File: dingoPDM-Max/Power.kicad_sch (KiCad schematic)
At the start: 14 parts, among them U1 VXO780x-500-M, U2 LD1117S33CTR

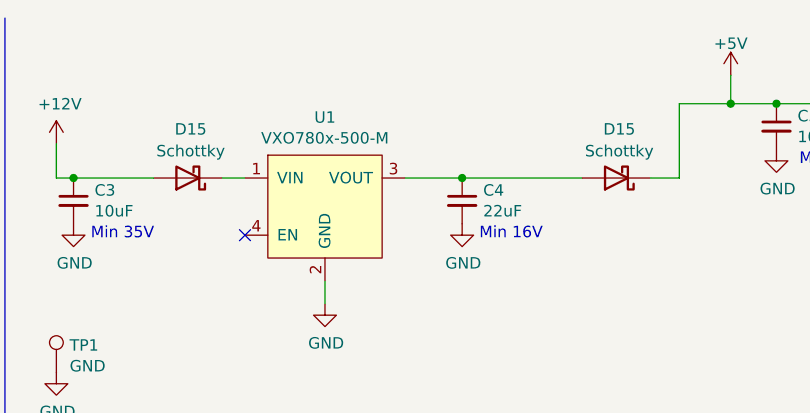
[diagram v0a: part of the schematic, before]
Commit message: Updated to Kicad 8
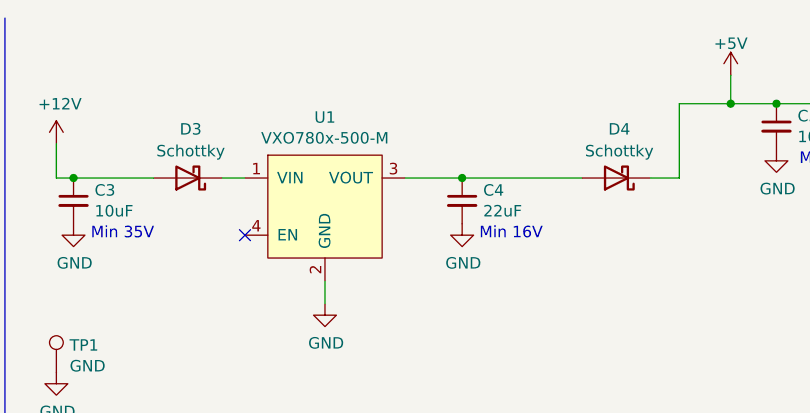
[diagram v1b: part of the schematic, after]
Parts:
- renumbered D15 to D3, D15 to D4

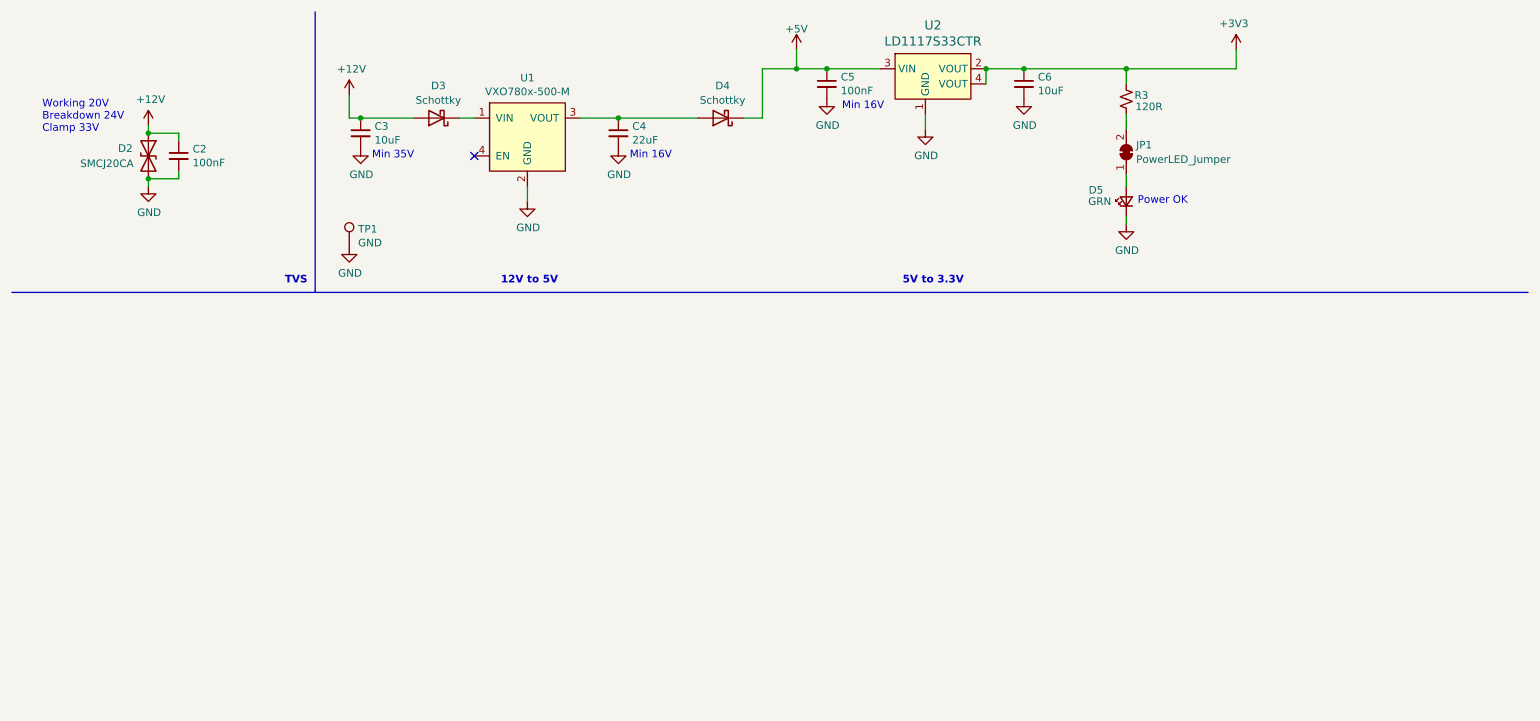
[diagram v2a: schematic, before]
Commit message: add dc-dc options and 5v cap
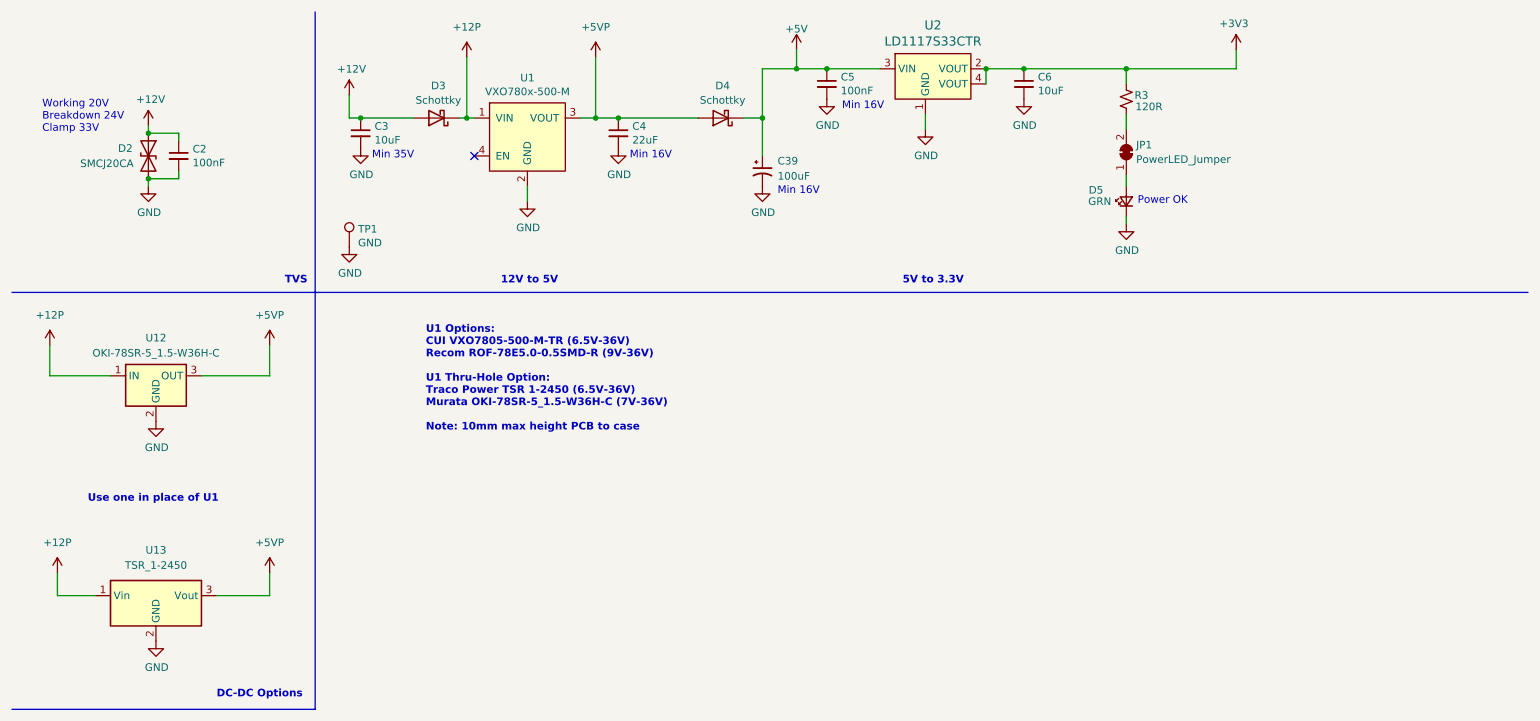
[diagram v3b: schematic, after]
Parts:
- added C39: 100uF, Capacitor_SMD:CP_Elec_6.3x7.7, symbol Device:C_Polarized_Small_US
- added U12: OKI-78SR-5_1.5-W36H-C, Converter_DCDC:Converter_DCDC_Murata_OKI-78SR_Horizontal, symbol Converter_DCDC:OKI-78SR-5_1.5-W36H-C
- added U13: TSR_1-2450, Converter_DCDC:Converter_DCDC_TRACO_TSR-1_THT, symbol Regulator_Switching:TSR_1-2450
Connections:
- net +5V: now also C39.1
- net GND: now also C39.2, U12.2 (GND), U13.2 (GND)
- net +12P: now reaches D3.1 (K), U1.1 (VIN)
- net +12P: now also U12.1 (IN), U13.1 (Vin)
- net +5VP: now reaches C4.1, D4.2 (A), U1.3 (VOUT)
- net +5VP: now also U12.3 (OUT), U13.3 (Vout)
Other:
- note added: "DC-DC Options"
- note added: "U1 Options: CUI VXO7805-500-M-TR (6.5V-36V) Recom ROF-78E5.0-0.5SMD-R (9V-36V) U1 Thru-Hole Option: Traco Power TSR 1-2450 (6.5V-36V) Murata OKI-78SR-5_1.5-W36H-C (7V-36V) Note: 10mm max height PCB to case"
- note added: "Use one in place of U1"

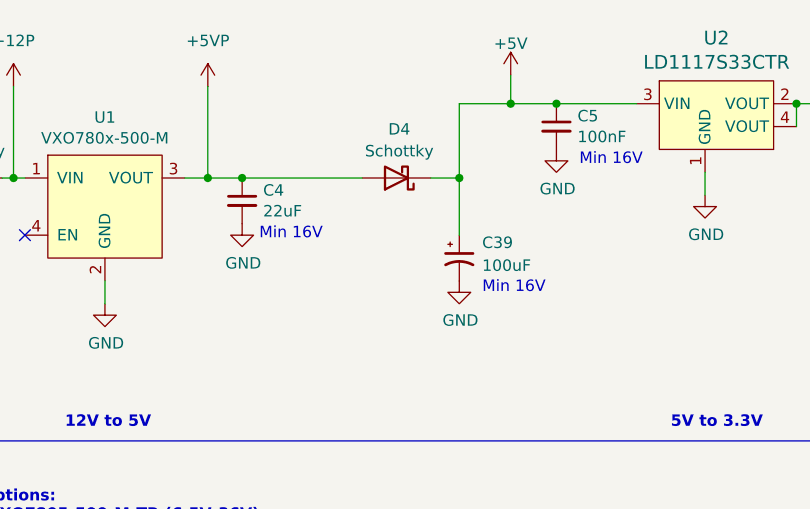
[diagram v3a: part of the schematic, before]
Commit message: switch to ceramic caps
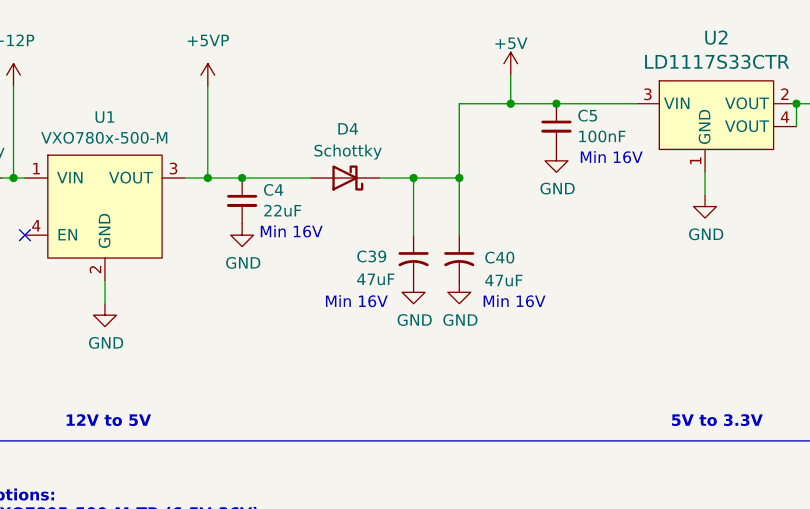
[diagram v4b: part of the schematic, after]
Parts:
- added C40: 47uF, Capacitor_SMD:C_2220_5750Metric, symbol Device:C_Small_US
- C39: value 100uF -> 47uF; footprint Capacitor_SMD:CP_Elec_6.3x7.7 -> Capacitor_SMD:C_2220_5750Metric; symbol Device:C_Polarized_Small_US -> Device:C_Small_US; Digi-Key_PN (none) -> 445-7935-1-ND
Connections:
- net +5V: now also C40.1
- net GND: now also C40.2
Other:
- moved on the sheet: D4
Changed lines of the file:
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@@
 	(text "Min 16V"
 		(exclude_from_sim no)
-		(at 140.97 44.704 0)
+		(at 123.444 46.482 0)
 		(effects
 			(font
@@
 		)
 	)
+	(text "Min 16V"
+		(exclude_from_sim no)
+		(at 140.97 46.482 0)
+		(effects
+			(font
+				(size 1.27 1.27)
+			)
+			(justify left bottom)
+		)
+	)
 	(text "DC-DC Options"
 		(exclude_from_sim no)
@@
 	)
 	(junction
+		(at 133.35 31.75)
+		(diameter 0)
+		(color 0 0 0 0)
+	)
+	(junction
 		(at 110.49 31.75)
 		(diameter 0)
@@
 	(wire
 		(pts
-			(xy 138.43 31.75) (xy 138.43 38.1)
+			(xy 133.35 31.75) (xy 133.35 38.1)
 		)
 		(stroke
@@
 	(wire
 		(pts
-			(xy 135.255 31.75) (xy 138.43 31.75)
+			(xy 129.54 31.75) (xy 133.35 31.75)
 		)
 		(stroke
@@
 		)
 	)
+	(wire
+		(pts
+			(xy 138.43 31.75) (xy 138.43 38.1)
+		)
+		(stroke
+			(width 0)
+			(type default)
+		)
+	)
 	(polyline
 		(pts
@@
 	(wire
 		(pts
-			(xy 114.3 31.75) (xy 127.635 31.75)
+			(xy 114.3 31.75) (xy 121.92 31.75)
 		)
 		(stroke
@@
 	(wire
 		(pts
+			(xy 133.35 31.75) (xy 138.43 31.75)
+		)
+		(stroke
+			(width 0)
+			(type default)
+		)
+	)
+	(wire
+		(pts
 			(xy 55.88 74.93) (xy 55.88 69.85)
 		)
@@
 	(symbol
 		(lib_id "Device:D_Schottky")
-		(at 131.445 31.75 180)
+		(at 125.73 31.75 180)
 		(unit 1)
 		(exclude_from_sim no)
@@
 		(fields_autoplaced yes)
 		(property "Reference" "D4"
-			(at 131.7625 26.3357 0)
+			(at 126.0475 26.3357 0)
 			(effects
 				(font
@@
 		)
 		(property "Value" "Schottky"
-			(at 131.7625 28.7599 0)
+			(at 126.0475 28.7599 0)
 			(effects
 				(font
@@
 		)
 		(property "Footprint" "Diode_SMD:D_SOD-123"
-			(at 131.445 31.75 0)
+			(at 125.73 31.75 0)
 			(effects
 				(font
@@
 		)
 		(property "Datasheet" ""
-			(at 131.445 31.75 0)
+			(at 125.73 31.75 0)
 			(effects
 				(font
@@
 		)
 		(property "Description" ""
-			(at 131.445 31.75 0)
+			(at 125.73 31.75 0)
 			(effects
 				(font
@@
 		)
 		(property "Digi-Key_PN" "1727-2394-1-ND"
-			(at 131.445 31.75 0)
+			(at 125.73 31.75 0)
 			(effects
 				(font
@@
 		)
 		(property "LCSC" "C179426"
-			(at 131.445 31.75 0)
+			(at 125.73 31.75 0)
 			(effects
 				(font
@@
 	)
 	(symbol
+		(lib_id "Device:C_Small_US")
+		(at 138.43 40.64 0)
+		(unit 1)
+		(exclude_from_sim no)
+		(in_bom yes)
+		(on_board yes)
+		(dnp no)
+		(property "Reference" "C40"
+			(at 141.224 40.64 0)
+			(effects
+				(font
+					(size 1.27 1.27)
+				)
+				(justify left)
+			)
+		)
+		(property "Value" "47uF"
+			(at 141.224 43.18 0)
+			(effects
+				(font
+					(size 1.27 1.27)
+				)
+				(justify left)
+			)
+		)
+		(property "Footprint" "Capacitor_SMD:C_2220_5750Metric"
+			(at 138.43 40.64 0)
+			(effects
+				(font
+					(size 1.27 1.27)
+				)
+				(hide yes)
+			)
+		)
+		(property "Datasheet" "~"
+			(at 138.43 40.64 0)
+			(effects
+				(font
+					(size 1.27 1.27)
+				)
+				(hide yes)
+			)
+		)
+		(property "Description" "capacitor, small US symbol"
+			(at 138.43 40.64 0)
+			(effects
+				(font
+					(size 1.27 1.27)
+				)
+				(hide yes)
+			)
+		)
+		(property "Digi-Key_PN" "445-7935-1-ND"
+			(at 138.43 40.64 0)
+			(effects
+				(font
+					(size 1.27 1.27)
+				)
+				(hide yes)
+			)
+		)
+		(pin "1"
+		)
+		(pin "2"
+		)
+		(instances
+			(project "dingoPDM-Max"
+				(path "/8948e307-9174-4227-9c28-3ff885e6e83d/00000000-0000-0000-0000-00005f5cf2eb"
+					(reference "C40")
+					(unit 1)
+				)
+			)
+		)
+	)
+	(symbol
 		(lib_id "power:+5V")
 		(at 144.145 20.32 0)
@@
 	)
 	(symbol
+		(lib_id "power:GND")
+		(at 138.43 43.18 0)
+		(unit 1)
+		(exclude_from_sim no)
+		(in_bom yes)
+		(on_board yes)
+		(dnp no)
+		(property "Reference" "#PWR099"
+			(at 138.43 49.53 0)
+			(effects
+				(font
+					(size 1.27 1.27)
+				)
+				(hide yes)
+			)
+		)
+		(property "Value" "GND"
+			(at 138.557 47.5742 0)
+			(effects
+				(font
+					(size 1.27 1.27)
+				)
+			)
+		)
+		(property "Footprint" ""
+			(at 138.43 43.18 0)
+			(effects
+				(font
+					(size 1.27 1.27)
+				)
+				(hide yes)
+			)
+		)
+		(property "Datasheet" ""
+			(at 138.43 43.18 0)
+			(effects
+				(font
+					(size 1.27 1.27)
+				)
+				(hide yes)
+			)
+		)
+		(property "Description" ""
+			(at 138.43 43.18 0)
+			(effects
+				(font
+					(size 1.27 1.27)
+				)
+				(hide yes)
+			)
+		)
+		(pin "1"
+		)
+		(instances
+			(project "dingoPDM-Max"
+				(path "/8948e307-9174-4227-9c28-3ff885e6e83d/00000000-0000-0000-0000-00005f5cf2eb"
+					(reference "#PWR099")
+					(unit 1)
+				)
+			)
+		)
+	)
+	(symbol
 		(lib_id "Jumper:SolderJumper_2_Bridged")
 		(at 199.39 37.465 90)
@@
 	)
 	(symbol
-		(lib_id "Device:C_Polarized_Small_US")
-		(at 138.43 40.64 0)
+		(lib_id "Device:C_Small_US")
+		(at 133.35 40.64 0)
 		(unit 1)
 		(exclude_from_sim no)
@@
 		(on_board yes)
 		(dnp no)
-		(fields_autoplaced yes)
 		(property "Reference" "C39"
-			(at 140.97 38.9381 0)
+			(at 127 40.5129 0)
 			(effects
 				(font
@@
 			)
 		)
-		(property "Value" "100uF"
-			(at 140.97 41.4781 0)
+		(property "Value" "47uF"
+			(at 127 43.0529 0)
 			(effects
 				(font
@@
 			)
 		)
-		(property "Footprint" "Capacitor_SMD:CP_Elec_6.3x7.7"
-			(at 138.43 40.64 0)
+		(property "Footprint" "Capacitor_SMD:C_2220_5750Metric"
+			(at 133.35 40.64 0)
 			(effects
 				(font
@@
 		)
 		(property "Datasheet" "~"
-			(at 138.43 40.64 0)
+			(at 133.35 40.64 0)
 			(effects
 				(font
@@
 			)
 		)
-		(property "Description" "Polarized capacitor, small US symbol"
-			(at 138.43 40.64 0)
+		(property "Description" "capacitor, small US symbol"
+			(at 133.35 40.64 0)
+			(effects
+				(font
+					(size 1.27 1.27)
+				)
+				(hide yes)
+			)
+		)
+		(property "Digi-Key_PN" "445-7935-1-ND"
+			(at 133.35 40.64 0)
 			(effects
 				(font
@@
 	(symbol
 		(lib_id "power:GND")
-		(at 138.43 43.18 0)
+		(at 133.35 43.18 0)
 		(unit 1)
 		(exclude_from_sim no)
@@
 		(dnp no)
 		(property "Reference" "#PWR094"
-			(at 138.43 49.53 0)
+			(at 133.35 49.53 0)
 			(effects
 				(font
@@
 		)
 		(property "Value" "GND"
-			(at 138.557 47.5742 0)
+			(at 133.477 47.5742 0)
 			(effects
 				(font
@@
 		)
 		(property "Footprint" ""
-			(at 138.43 43.18 0)
+			(at 133.35 43.18 0)
 			(effects
 				(font
@@
 		)
 		(property "Datasheet" ""
-			(at 138.43 43.18 0)
+			(at 133.35 43.18 0)
 			(effects
 				(font
@@
 		)
 		(property "Description" ""
-			(at 138.43 43.18 0)
+			(at 133.35 43.18 0)
 			(effects
 				(font

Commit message: fixed bad zone, shifted traces, increase trace widths
update part numbers for ibom
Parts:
- C39, C40: LCSC (none) -> C22388555
- U1: LCSC (none) -> C5137464
- U12: Digi-Key_PN (none) -> 811-2692-ND; LCSC (none) -> C266374
- U13: Digi-Key_PN (none) -> 1951-2747-ND; LCSC (none) -> C6886877
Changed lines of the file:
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@@
 	(title_block
 		(title "dingoPDM-Max")
-		(date "2025-06-16")
-		(rev "v1.1")
+		(date "2025-09-29")
+		(rev "v1.2")
 		(comment 3 "github.com/corygrant")
 		(comment 4 "Cory Grant")
@@
 			)
 		)
-		(property "LCSC" ""
+		(property "LCSC" "C5137464"
 			(at 99.06 34.29 0)
 			(effects
@@
 			)
 		)
+		(property "LCSC" "C22388555"
+			(at 138.43 40.64 0)
+			(effects
+				(font
+					(size 1.27 1.27)
+				)
+				(hide yes)
+			)
+		)
 		(pin "1"
 		)
@@
 			)
 		)
+		(property "Digi-Key_PN" "1951-2747-ND"
+			(at 36.83 114.3 0)
+			(effects
+				(font
+					(size 1.27 1.27)
+				)
+				(hide yes)
+			)
+		)
+		(property "LCSC" "C6886877"
+			(at 36.83 114.3 0)
+			(effects
+				(font
+					(size 1.27 1.27)
+				)
+				(hide yes)
+			)
+		)
 		(pin "2"
 		)
@@
 			)
 		)
+		(property "LCSC" "C22388555"
+			(at 133.35 40.64 0)
+			(effects
+				(font
+					(size 1.27 1.27)
+				)
+				(hide yes)
+			)
+		)
 		(pin "1"
 		)
@@
 			(at 36.83 74.93 0)
 			(effects
+				(font
+					(size 1.27 1.27)
+				)
+				(hide yes)
+			)
+		)
+		(property "Digi-Key_PN" "811-2692-ND"
+			(at 36.83 74.93 0)
+			(effects
+				(font
+					(size 1.27 1.27)
+				)
+				(hide yes)
+			)
+		)
+		(property "LCSC" "C266374"
+			(at 36.83 74.93 0)
+			(effects
